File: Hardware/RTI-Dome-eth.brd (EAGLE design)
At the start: 119.4 x 71.1 mm, 81 parts, among them IC1 24AA128ST, IC3 FT232RL, IC5 74LVC245, IC6 74ABT245, J1 POWERPOLE_POWER45A, U1 W5500, X13 PN61729-S, X9 J1011F21PNL

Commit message: Fix pin spacing issue.
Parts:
- moved J1 2.54 mm to (102.9, 8.89)
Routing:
- net +12V: track 210.6 -> 213.1 mm, vias 44 -> 33
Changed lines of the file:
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@@
 <setting verticaltext="up"/>
 </settings>
-<grid distance="1.27" unitdist="mm" unit="mm" style="lines" multiple="1" display="yes" altdistance="0.03175" altunitdist="mm" altunit="mm"/>
+<grid distance="1.27" unitdist="mm" unit="mm" style="lines" multiple="1" display="yes" altdistance="0.01" altunitdist="mm" altunit="mm"/>
 <layers>
 <layer number="1" name="Top" color="4" fill="1" visible="yes" active="yes"/>
@@
 <param name="mvStopFrame" value="1"/>
 <param name="mvCreamFrame" value="0"/>
-<param name="mlMinStopFrame" value="3mil"/>
+<param name="mlMinStopFrame" value="0mil"/>
 <param name="mlMaxStopFrame" value="3mil"/>
 <param name="mlMinCreamFrame" value="0mil"/>
-<param name="mlMaxCreamFrame" value="0mil"/>
+<param name="mlMaxCreamFrame" value="3mil"/>
 <param name="mlViaStopLimit" value="130mil"/>
 <param name="srRoundness" value="0"/>
@@
 <element name="R39" library="rti" package="R0805" value="12.4K 1%" x="77.47" y="34.95675"/>
 <element name="R40" library="rti" package="R0805" value="4.7K" x="63.1825" y="41.91" rot="R270"/>
-<element name="J1" library="powerpoles" package="POWERPOLE_PAIR_45A" value="POWERPOLE_POWER45A" x="102.87" y="11.43" rot="MR90"/>
+<element name="J1" library="powerpoles" package="POWERPOLE_PAIR_45A" value="POWERPOLE_POWER45A" x="102.87" y="8.89" rot="MR90"/>
 <element name="25MHZ" library="rti" package="CB3" value="CB3LV-OSCILATOR" x="58.42" y="27.94"/>
 <element name="C20" library="rti" package="C0805" value="100nF" x="53.34" y="27.94" rot="R90"/>
@@
 <polygon width="0.3048" layer="1" thermals="no">
 <vertex x="82.55" y="8.89"/>
-<vertex x="87.63" y="8.89"/>
-<vertex x="95.25" y="11.43"/>
-<vertex x="119.38" y="11.43"/>
+<vertex x="119.38" y="8.89"/>
 <vertex x="119.38" y="0"/>
 <vertex x="82.55" y="0"/>
@@
 <contactref element="R10" pad="2"/>
 <wire x1="25.4" y1="69.85" x2="115.57" y2="69.85" width="1.27" layer="1"/>
-<wire x1="118.11" y1="67.31" x2="118.11" y2="10.16" width="1.27" layer="1"/>
+<wire x1="118.11" y1="67.31" x2="118.11" y2="7.62" width="1.27" layer="1"/>
 <contactref element="C3" pad="1"/>
 <wire x1="23.9268" y1="66.04" x2="23.9268" y2="68.3768" width="1.27" layer="1"/>
@@
 <wire x1="25.4" y1="69.85" x2="23.9268" y2="68.3768" width="1.27" layer="1" curve="90"/>
 <polygon width="0.254" layer="16" thermals="no">
-<vertex x="95.25" y="11.43"/>
-<vertex x="119.38" y="11.43"/>
+<vertex x="82.55" y="8.89"/>
+<vertex x="119.38" y="8.89"/>
 <vertex x="119.38" y="0"/>
 <vertex x="82.55" y="0"/>
-<vertex x="82.55" y="8.89"/>
-<vertex x="87.63" y="8.89"/>
 </polygon>
 <via x="107.95" y="5.08" extent="1-16" drill="0.4" diameter="1.27"/>
-<via x="97.79" y="10.16" extent="1-16" drill="0.4" diameter="1.27"/>
 <via x="105.41" y="7.62" extent="1-16" drill="0.4" diameter="1.27"/>
 <via x="107.95" y="7.62" extent="1-16" drill="0.4" diameter="1.27"/>
@@
 <via x="113.03" y="7.62" extent="1-16" drill="0.4" diameter="1.27"/>
 <via x="115.57" y="7.62" extent="1-16" drill="0.4" diameter="1.27"/>
-<via x="118.11" y="10.16" extent="1-16" drill="0.4" diameter="1.27"/>
-<via x="100.33" y="10.16" extent="1-16" drill="0.4" diameter="1.27"/>
+<via x="118.11" y="7.62" extent="1-16" drill="0.4" diameter="1.27"/>
 <via x="100.33" y="7.62" extent="1-16" drill="0.4" diameter="1.27"/>
 <wire x1="34.9225" y1="13.5255" x2="34.925" y2="13.5255" width="0.8128" layer="1"/>
@@
 <wire x1="34.9885" y1="8.60175" x2="34.9885" y2="10.9855" width="1.6764" layer="1"/>
 <wire x1="34.9885" y1="10.9855" x2="34.95675" y2="11.01725" width="1.6764" layer="1"/>
-<via x="105.41" y="10.16" extent="1-16" drill="0.4" diameter="1.27"/>
-<via x="107.95" y="10.16" extent="1-16" drill="0.4" diameter="1.27"/>
-<via x="110.49" y="10.16" extent="1-16" drill="0.4" diameter="1.27"/>
-<via x="113.03" y="10.16" extent="1-16" drill="0.4" diameter="1.27"/>
-<via x="115.57" y="10.16" extent="1-16" drill="0.4" diameter="1.27"/>
-<via x="118.11" y="7.62" extent="1-16" drill="0.4" diameter="1.27"/>
 <via x="100.33" y="2.54" extent="1-16" drill="0.4" diameter="1.27"/>
-<via x="102.87" y="2.54" extent="1-16" drill="0.4" diameter="1.27"/>
 <via x="97.79" y="2.54" extent="1-16" drill="0.4" diameter="1.27"/>
-<via x="95.25" y="10.16" extent="1-16" drill="0.4" diameter="1.27"/>
 <via x="95.25" y="2.54" extent="1-16" drill="0.4" diameter="1.27"/>
 <via x="92.71" y="2.54" extent="1-16" drill="0.4" diameter="1.27"/>
-<via x="92.71" y="8.89" extent="1-16" drill="0.4" diameter="1.27"/>
 <via x="90.17" y="5.08" extent="1-16" drill="0.4" diameter="1.27"/>
 <via x="87.63" y="2.54" extent="1-16" drill="0.4" diameter="1.27"/>

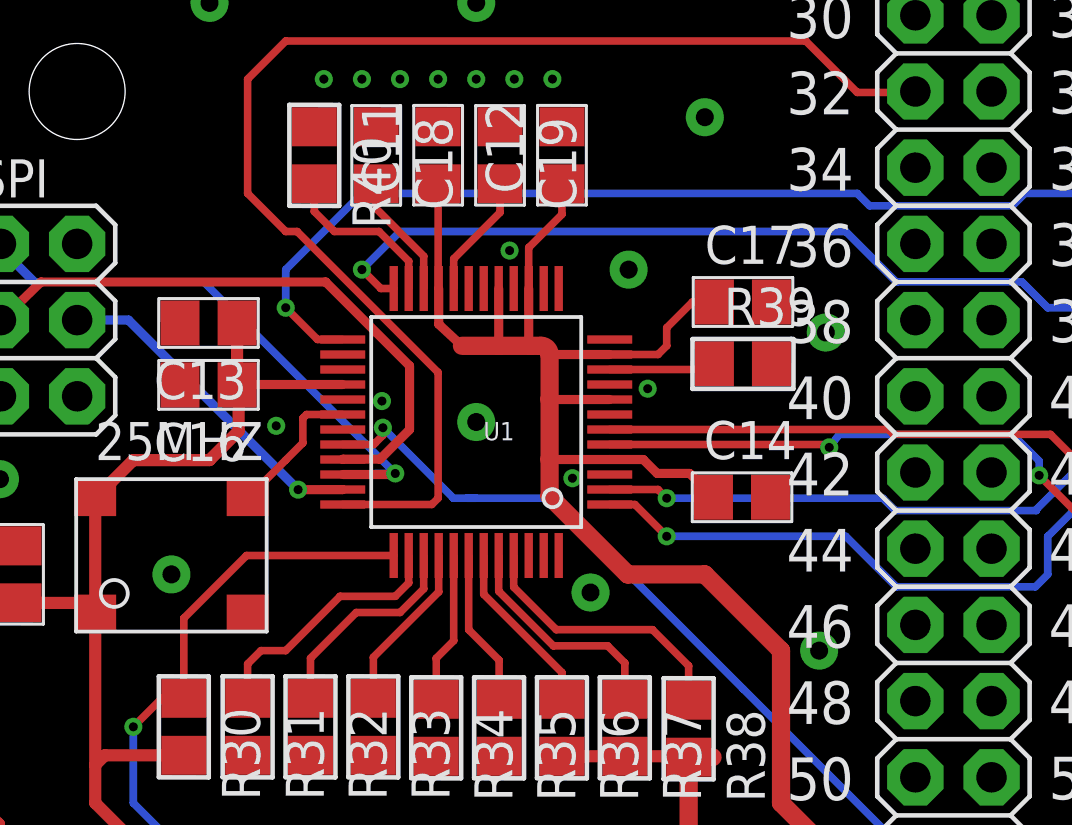
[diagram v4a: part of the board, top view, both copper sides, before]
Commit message: Fix W5500 package for PCB house
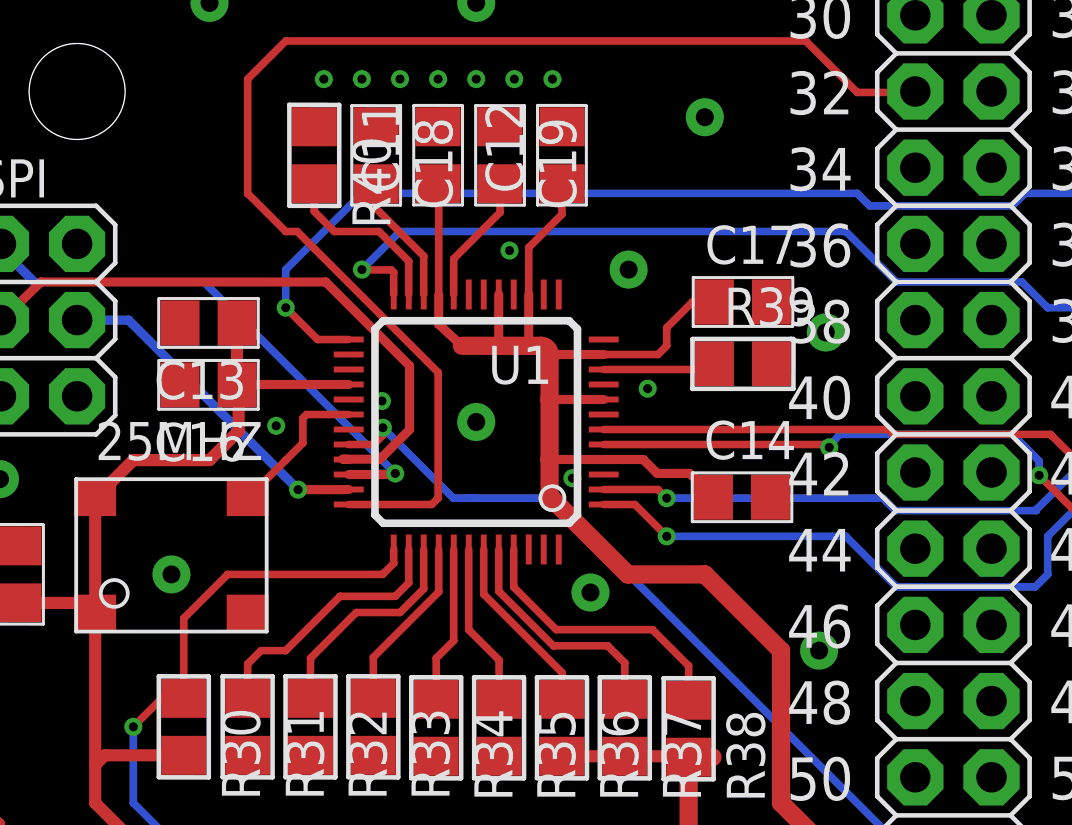
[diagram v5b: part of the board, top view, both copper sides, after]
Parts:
- U1: device W5500:W5500 -> W5500:LQFP48
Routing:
- net SPD_100: track 45.1 -> 45.6 mm

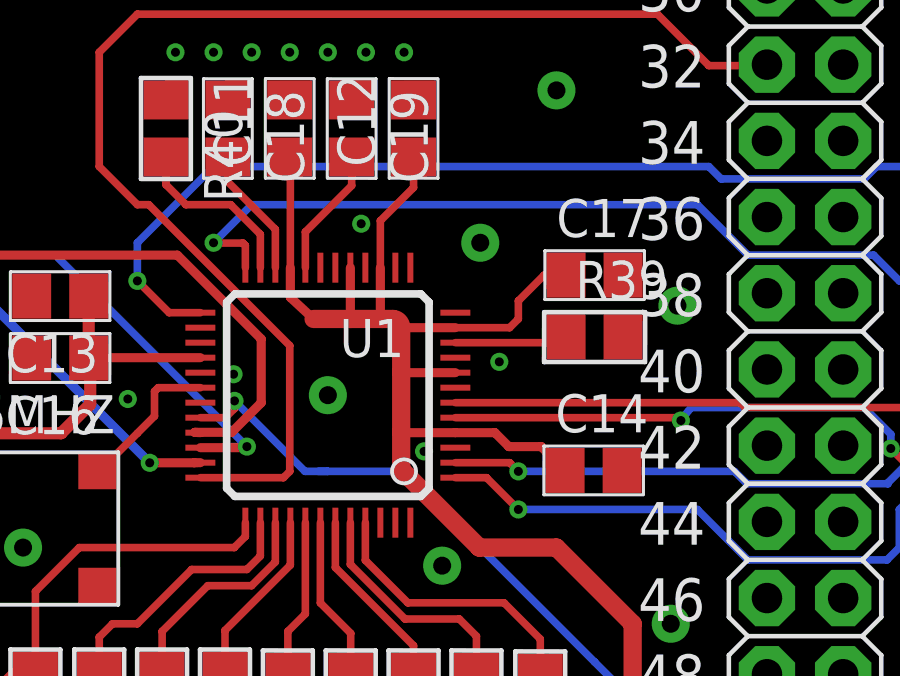
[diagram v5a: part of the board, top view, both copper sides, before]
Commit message: Fix some pin routing to optimize path
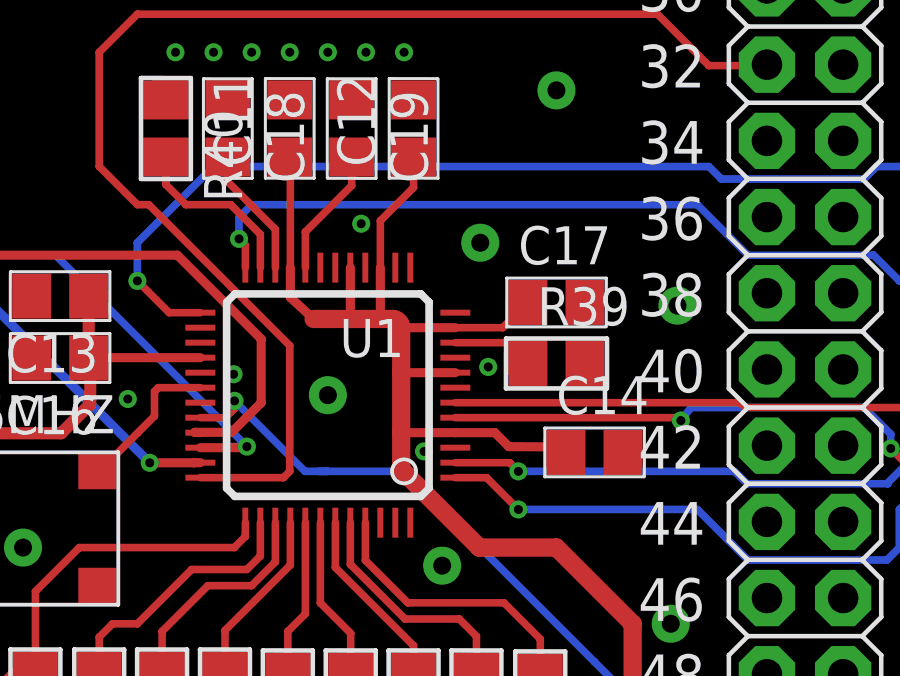
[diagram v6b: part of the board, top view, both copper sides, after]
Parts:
- moved C17 1.56 mm to (76.2, 36.1)
- moved R39 1.55 mm to (76.2, 34.1)
- moved C14 0.60 mm to (77.5, 31.1)
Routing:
- net AVDD: track 93.4 -> 91.2 mm
- net SPD_100: track 45.6 -> 44.3 mm
- net N$34: track 3.77 -> 2.71 mm
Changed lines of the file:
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@@
 <param name="mdDrill" value="6mil"/>
 <param name="mdSmdStop" value="0mil"/>
-<param name="msWidth" value="8mil"/>
+<param name="msWidth" value="6mil"/>
 <param name="msDrill" value="0.3mm"/>
 <param name="msMicroVia" value="8mil"/>
@@
 <element name="C11" library="rti" package="C0805" value="100nF" x="67.31" y="41.91" rot="R90"/>
 <element name="C12" library="rti" package="C0805" value="100nF" x="71.4375" y="41.91" rot="R90"/>
-<element name="C14" library="rti" package="C0805" value="100nF" x="77.43825" y="30.51175"/>
+<element name="C14" library="rti" package="C0805" value="100nF" x="77.46825" y="31.11175"/>
 <element name="C16" library="rti" package="C0805" value="100nF" x="59.65825" y="34.25825" rot="R180"/>
-<element name="C17" library="rti" package="C0805" value="100nF" x="77.47" y="37.0205"/>
+<element name="C17" library="rti" package="C0805" value="100nF" x="76.2" y="36.1105"/>
 <element name="C18" library="rti" package="C0805" value="10nF" x="65.24625" y="41.91" rot="R270"/>
 <element name="R28" library="rti" package="R0805" value="330" x="97.79" y="24.13" rot="R270"/>
 <element name="R29" library="rti" package="R0805" value="330" x="96.52" y="36.83" rot="R180"/>
 <element name="C19" library="rti" package="C0805" value="4.7uF" x="69.37375" y="41.91" rot="R270"/>
-<element name="R39" library="rti" package="R0805" value="12.4K 1%" x="77.47" y="34.95675"/>
+<element name="R39" library="rti" package="R0805" value="12.4K 1%" x="76.2" y="34.07675"/>
 <element name="R40" library="rti" package="R0805" value="4.7K" x="63.1825" y="41.91" rot="R270"/>
 <element name="J1" library="powerpoles" package="POWERPOLE_PAIR_45A" value="POWERPOLE_POWER45A" x="102.87" y="8.89" rot="MR90"/>
@@
 <contactref element="25MHZ" pad="2"/>
 <contactref element="C20" pad="2"/>
-<via x="74.295" y="34.13125" extent="1-16" drill="0.3"/>
+<via x="73.925" y="33.96125" extent="1-16" drill="0.3"/>
 <via x="80.23225" y="36.0045" extent="1-16" drill="0.6" diameter="1.27"/>
 <via x="113.03" y="34.29" extent="1-16" drill="0.6" diameter="1.27"/>
@@
 <contactref element="X9" pad="11"/>
 <contactref element="U1" pad="24"/>
-<via x="64.77" y="38.1" extent="1-16" drill="0.3"/>
-<wire x1="64.77" y1="38.1" x2="66.04" y2="39.37" width="0.254" layer="16"/>
-<wire x1="66.04" y1="39.37" x2="80.899" y2="39.37" width="0.254" layer="16"/>
+<via x="65.62" y="38.23" extent="1-16" drill="0.3"/>
 <wire x1="80.899" y1="39.37" x2="82.58175" y2="37.68725" width="0.254" layer="16"/>
 <wire x1="82.58175" y1="37.68725" x2="86.77275" y2="37.68725" width="0.254" layer="16"/>
@@
 <wire x1="99.06" y1="35.56" x2="99.06" y2="30.345" width="0.254" layer="16"/>
 <wire x1="99.06" y1="30.345" x2="100.58" y2="28.825" width="0.254" layer="16"/>
-<wire x1="65.83" y1="37.27" x2="65.83" y2="38.01" width="0.254" layer="1"/>
-<wire x1="65.83" y1="38.01" x2="65.75" y2="38.09" width="0.254" layer="1"/>
-<wire x1="65.75" y1="38.09" x2="64.78" y2="38.09" width="0.254" layer="1"/>
-<wire x1="64.78" y1="38.09" x2="64.77" y2="38.1" width="0.254" layer="1"/>
+<wire x1="66.04" y1="39.37" x2="80.899" y2="39.37" width="0.254" layer="16"/>
+<wire x1="65.83" y1="37.27" x2="65.83" y2="38.02" width="0.254" layer="1"/>
+<wire x1="65.83" y1="38.02" x2="65.62" y2="38.23" width="0.254" layer="1"/>
+<wire x1="66.04" y1="39.37" x2="65.62" y2="38.95" width="0.254" layer="16"/>
+<wire x1="65.62" y1="38.95" x2="65.62" y2="38.23" width="0.254" layer="16"/>
 </signal>
 <signal name="LINK_ACK">
@@
 <contactref element="U1" pad="10"/>
 <contactref element="R39" pad="1"/>
-<wire x1="72.83" y1="34.77" x2="76.33325" y2="34.77" width="0.254" layer="1"/>
-<wire x1="76.33325" y1="34.77" x2="76.52" y2="34.95675" width="0.254" layer="1"/>
+<wire x1="72.83" y1="34.77" x2="74.55675" y2="34.77" width="0.254" layer="1"/>
+<wire x1="74.55675" y1="34.77" x2="75.25" y2="34.07675" width="0.254" layer="1"/>
 </signal>
 <signal name="N$35">
@@
 <contactref element="C17" pad="1"/>
 <wire x1="74.148" y1="31.77" x2="74.6125" y2="31.3055" width="0.3048" layer="1"/>
-<wire x1="74.6125" y1="31.3055" x2="75.6945" y2="31.3055" width="0.3048" layer="1"/>
-<wire x1="75.6945" y1="31.3055" x2="76.48825" y2="30.51175" width="0.3048" layer="1"/>
-<wire x1="74.64" y1="35.27" x2="74.93" y2="35.56" width="0.254" layer="1"/>
-<wire x1="74.93" y1="35.56" x2="74.93" y2="36.16325" width="0.254" layer="1"/>
-<wire x1="74.93" y1="36.16325" x2="75.78725" y2="37.0205" width="0.254" layer="1"/>
-<wire x1="75.78725" y1="37.0205" x2="76.52" y2="37.0205" width="0.254" layer="1"/>
+<wire x1="74.6125" y1="31.3055" x2="76.0245" y2="31.2955" width="0.3048" layer="1"/>
+<wire x1="76.0245" y1="31.2955" x2="76.51825" y2="31.11175" width="0.3048" layer="1"/>
 <wire x1="67.33" y1="40.94" x2="67.31" y2="40.96" width="0.3048" layer="1"/>
 <wire x1="67.33" y1="40.94" x2="67.31" y2="40.96" width="0.254" layer="1"/>
@@
 <wire x1="70.33" y1="38.834" x2="71.4375" y2="39.9415" width="0.254" layer="1"/>
 <wire x1="71.4375" y1="39.9415" x2="71.4375" y2="40.96" width="0.254" layer="1"/>
-<wire x1="72.83" y1="35.27" x2="74.64" y2="35.27" width="0.254" layer="1"/>
 <wire x1="72.83" y1="31.77" x2="74.148" y2="31.77" width="0.3048" layer="1"/>
 <contactref element="R27" pad="2"/>
@@
 <wire x1="67.33" y1="37.27" x2="67.33" y2="40.94" width="0.254" layer="1"/>
 <wire x1="67.33" y1="40.94" x2="67.31" y2="40.96" width="0.254" layer="1"/>
+<wire x1="72.83" y1="35.27" x2="74.4095" y2="35.27" width="0.254" layer="1"/>
+<wire x1="74.4095" y1="35.27" x2="75.25" y2="36.1105" width="0.254" layer="1"/>
 </signal>
 </signals>
